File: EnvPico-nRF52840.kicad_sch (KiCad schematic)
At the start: 48 parts, among them J3 2.54mm header 01x20, J4 2.54mm header 01x20, J5 Conn_01x03_Male, U1 LM3671MF 3.3, U2 BQ24072RGT, U3 nRF52840, Y1 32MHz 12pF

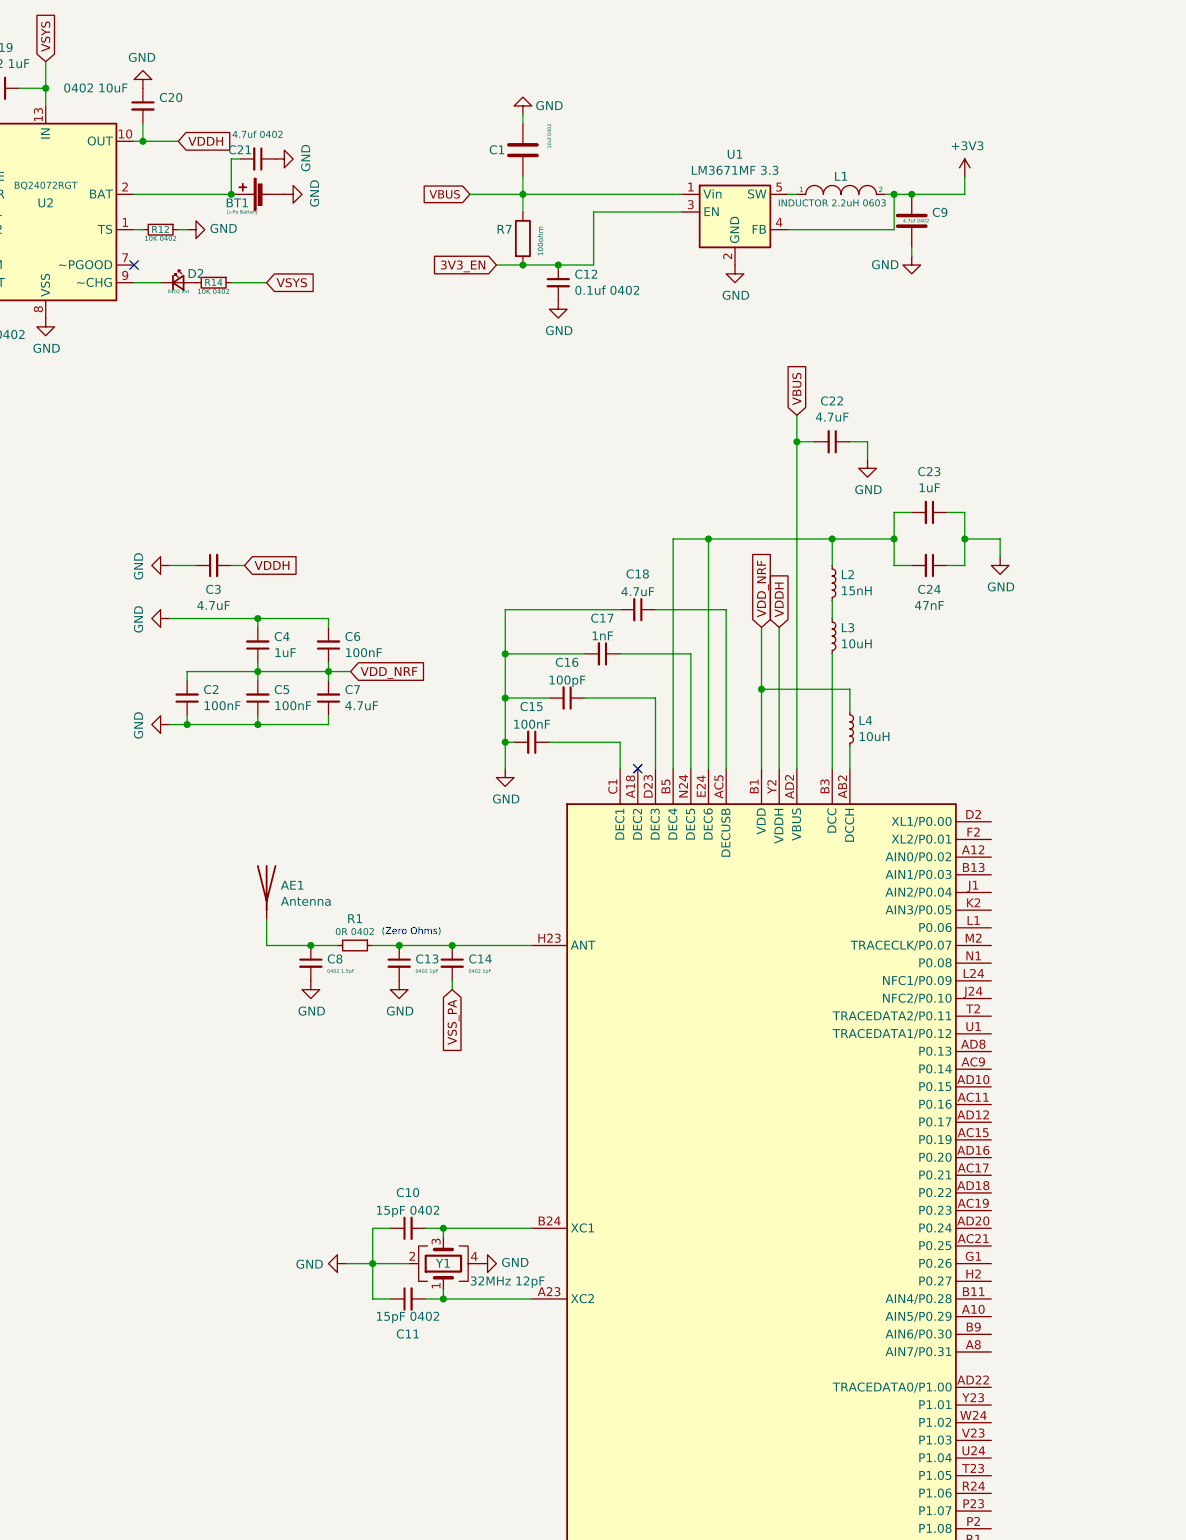
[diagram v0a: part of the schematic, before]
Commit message: started adding some pins for GPIO
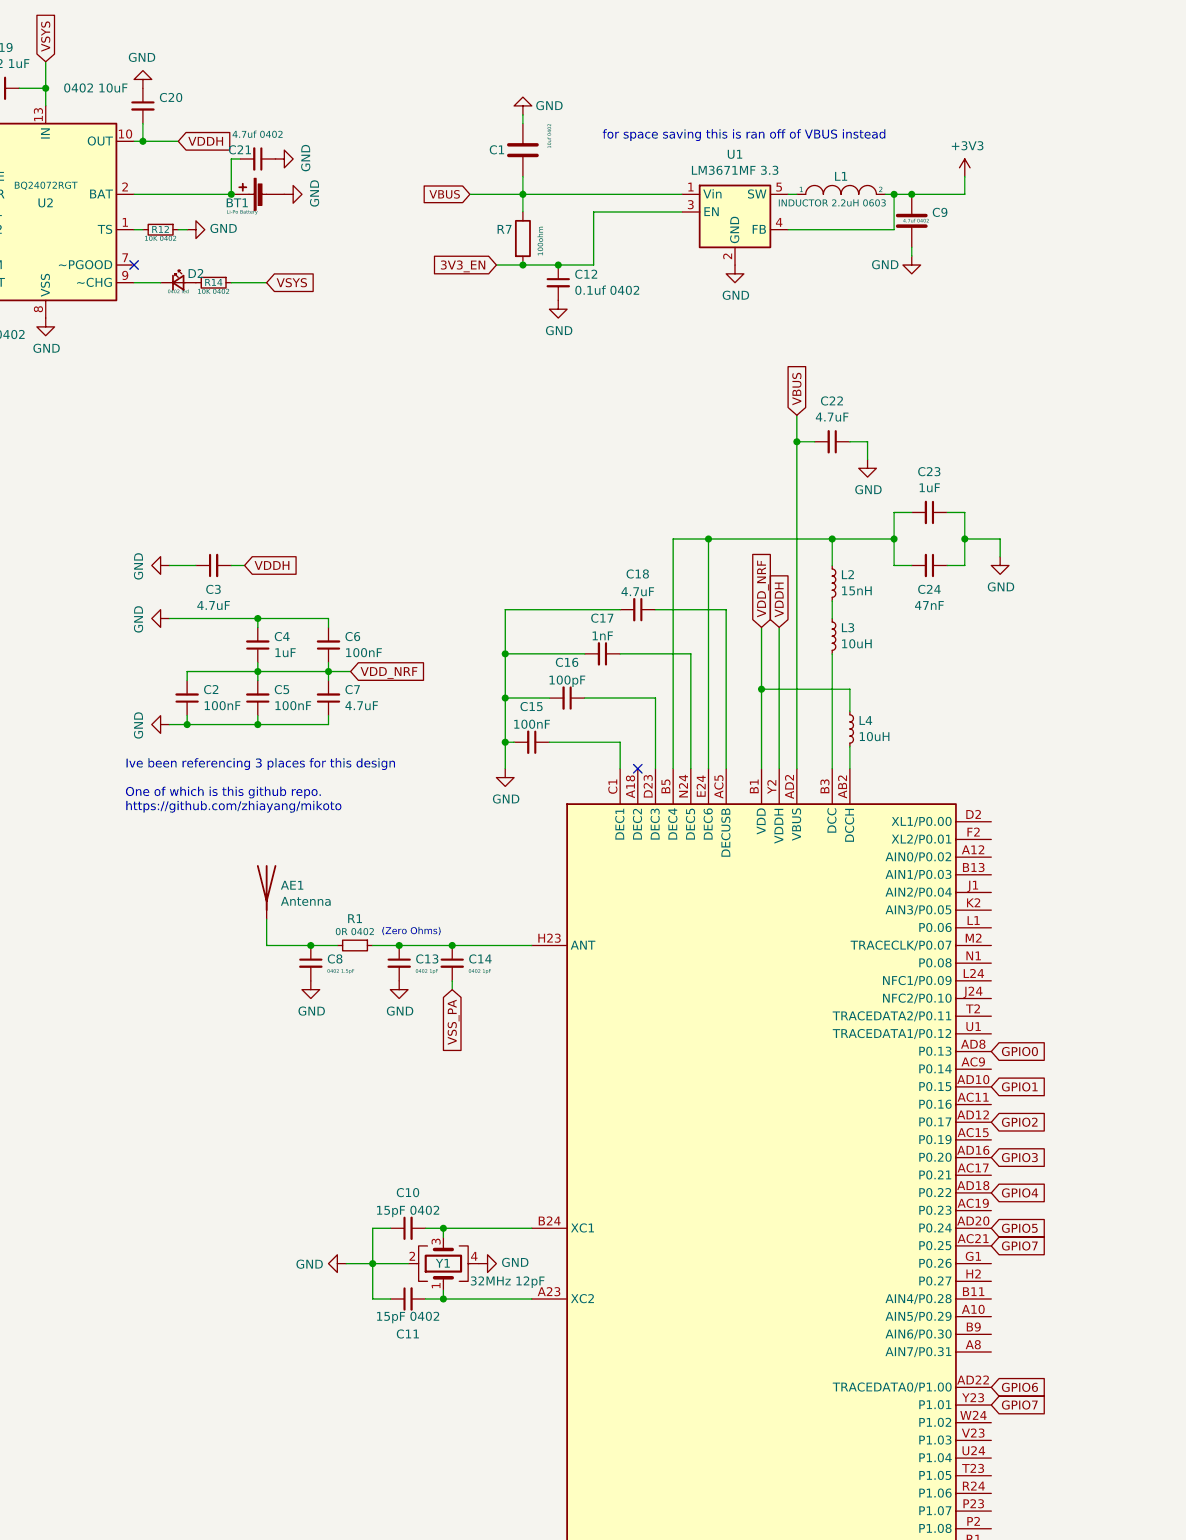
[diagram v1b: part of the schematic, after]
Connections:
- net GPIO7: now reaches U3.AC21 (P0.25)
- net GPIO7: now also U3.Y23 (P1.01)
- net GPIO1: now reaches U3.AD10 (P0.15)
- net GPIO2: now reaches U3.AD12 (P0.17)
- net GPIO3: now reaches U3.AD16 (P0.20)
- net GPIO4: now reaches U3.AD18 (P0.22)
- net GPIO5: now reaches U3.AD20 (P0.24)
- net GPIO6: now reaches U3.AD22 (TRACEDATA0/P1.00)
- net GPIO0: now reaches U3.AD8 (P0.13)
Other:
- note added: "Ive been referencing 3 places for this design One of which is this github repo. https://github.com/zhiayang/mikoto"
- note added: "for space saving this is ran off of VBUS instead"
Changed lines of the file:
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@@
     (effects (font (size 0.508 0.508)) (justify left bottom))
+  )
+  (text "Ive been referencing 3 places for this design\n\nOne of which is this github repo.\nhttps://github.com/zhiayang/mikoto"
+    (at 114.3 135.89 0)
+    (effects (font (size 1.27 1.27)) (justify left bottom))
   )
   (text "(Zero Ohms)" (at 151.13 153.67 0)
     (effects (font (size 0.9906 0.9906)) (justify left bottom))
+  )
+  (text "for space saving this is ran off of VBUS instead" (at 182.88 39.37 0)
+    (effects (font (size 1.27 1.27)) (justify left bottom))
   )
   (text "GPIOs" (at 347.98 114.3 0)
@@
     )
   )
+  (global_label "GPIO0" (shape input) (at 238.76 170.18 0) (fields_autoplaced)
+    (effects (font (size 1.27 1.27)) (justify left))
+    (property "Intersheet References" "${INTERSHEET_REFS}" (id 0) (at 246.7182 170.1006 0)
+      (effects (font (size 1.27 1.27)) (justify left) hide)
+    )
+  )
+  (global_label "GPIO1" (shape input) (at 238.76 175.26 0) (fields_autoplaced)
+    (effects (font (size 1.27 1.27)) (justify left))
+    (property "Intersheet References" "${INTERSHEET_REFS}" (id 0) (at 246.7182 175.1806 0)
+      (effects (font (size 1.27 1.27)) (justify left) hide)
+    )
+  )
+  (global_label "GPIO2" (shape input) (at 238.76 180.34 0) (fields_autoplaced)
+    (effects (font (size 1.27 1.27)) (justify left))
+    (property "Intersheet References" "${INTERSHEET_REFS}" (id 0) (at 246.7182 180.2606 0)
+      (effects (font (size 1.27 1.27)) (justify left) hide)
+    )
+  )
+  (global_label "GPIO3" (shape input) (at 238.76 185.42 0) (fields_autoplaced)
+    (effects (font (size 1.27 1.27)) (justify left))
+    (property "Intersheet References" "${INTERSHEET_REFS}" (id 0) (at 246.7182 185.3406 0)
+      (effects (font (size 1.27 1.27)) (justify left) hide)
+    )
+  )
+  (global_label "GPIO4" (shape input) (at 238.76 190.5 0) (fields_autoplaced)
+    (effects (font (size 1.27 1.27)) (justify left))
+    (property "Intersheet References" "${INTERSHEET_REFS}" (id 0) (at 246.7182 190.4206 0)
+      (effects (font (size 1.27 1.27)) (justify left) hide)
+    )
+  )
+  (global_label "GPIO5" (shape input) (at 238.76 195.58 0) (fields_autoplaced)
+    (effects (font (size 1.27 1.27)) (justify left))
+    (property "Intersheet References" "${INTERSHEET_REFS}" (id 0) (at 246.7182 195.5006 0)
+      (effects (font (size 1.27 1.27)) (justify left) hide)
+    )
+  )
+  (global_label "GPIO7" (shape input) (at 238.76 198.12 0) (fields_autoplaced)
+    (effects (font (size 1.27 1.27)) (justify left))
+    (property "Intersheet References" "${INTERSHEET_REFS}" (id 0) (at 246.7182 198.0406 0)
+      (effects (font (size 1.27 1.27)) (justify left) hide)
+    )
+  )
+  (global_label "GPIO6" (shape input) (at 238.76 218.44 0) (fields_autoplaced)
+    (effects (font (size 1.27 1.27)) (justify left))
+    (property "Intersheet References" "${INTERSHEET_REFS}" (id 0) (at 246.7182 218.3606 0)
+      (effects (font (size 1.27 1.27)) (justify left) hide)
+    )
+  )
+  (global_label "GPIO7" (shape input) (at 238.76 220.98 0) (fields_autoplaced)
+    (effects (font (size 1.27 1.27)) (justify left))
+    (property "Intersheet References" "${INTERSHEET_REFS}" (id 0) (at 246.7182 220.9006 0)
+      (effects (font (size 1.27 1.27)) (justify left) hide)
+    )
+  )

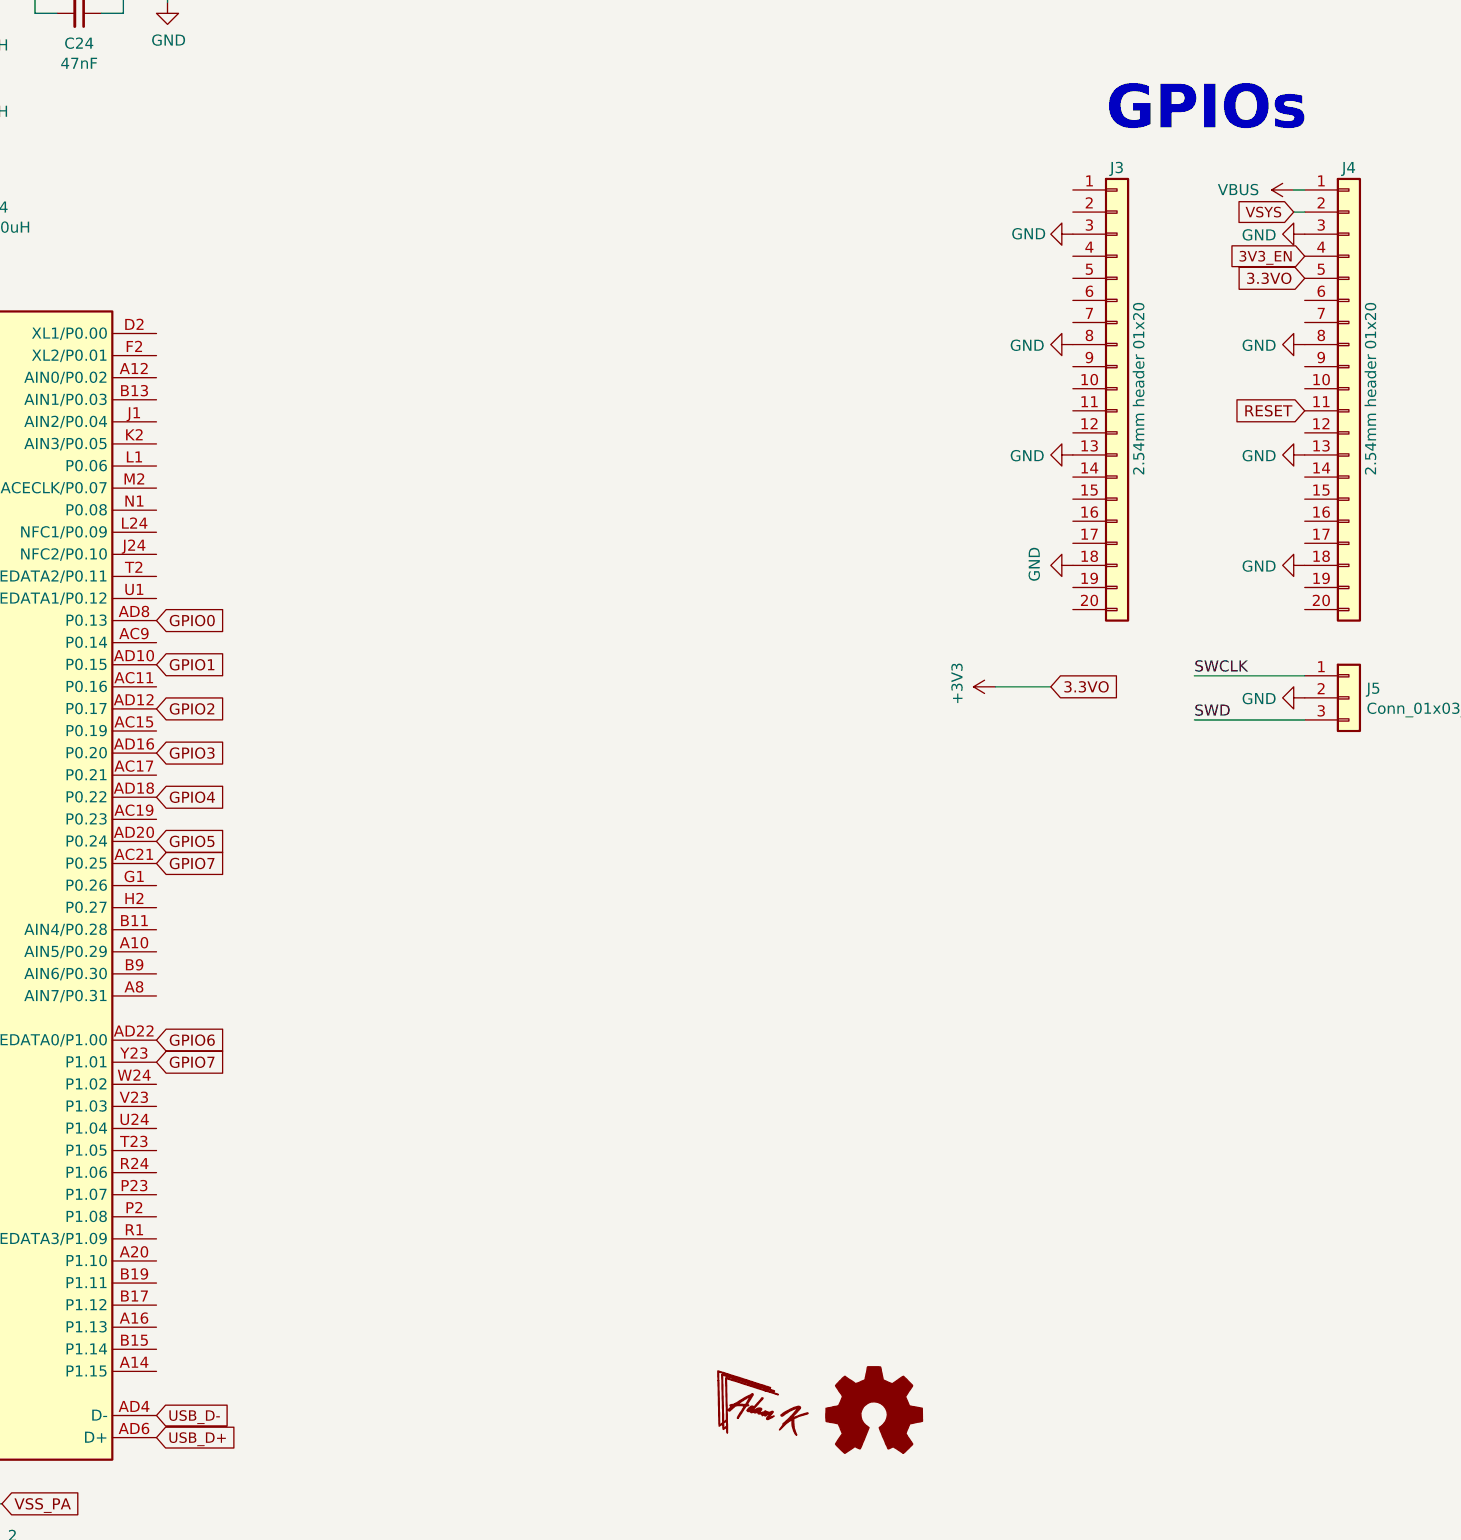
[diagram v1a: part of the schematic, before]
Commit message: connected all 26 GPIOs among other things.
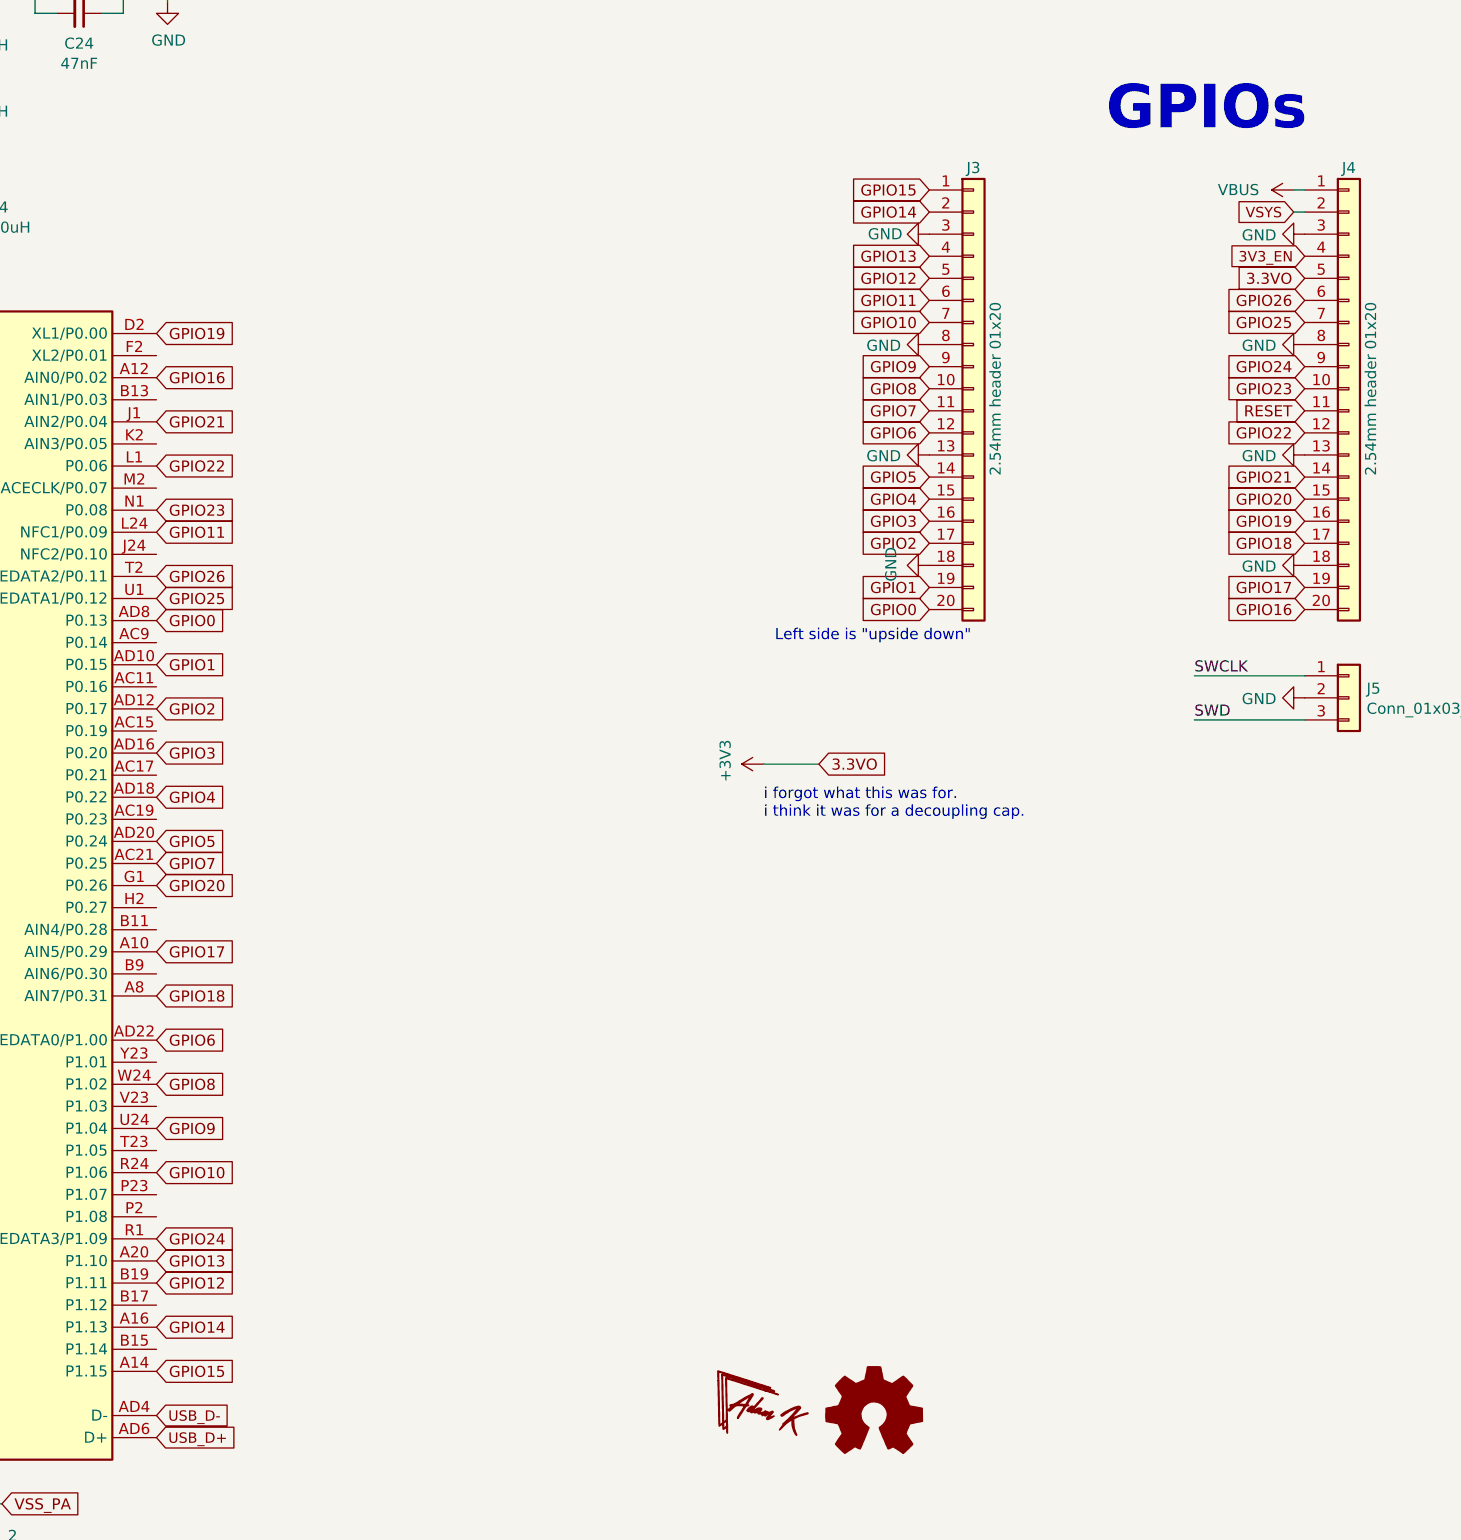
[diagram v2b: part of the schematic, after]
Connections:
- net GPIO0: now also J3.20 (Pin_20)
- net GPIO1: now also J3.19 (Pin_19)
- net GPIO2: now also J3.17 (Pin_17)
- net GPIO3: now also J3.16 (Pin_16)
- net GPIO4: now also J3.15 (Pin_15)
- net GPIO5: now also J3.14 (Pin_14)
- net GPIO6: now also J3.12 (Pin_12)
- net GPIO7: now also J3.11 (Pin_11); no longer U3.Y23 (P1.01)
- net GPIO23: now reaches J4.10 (Pin_10)
- net GPIO23: now also U3.N1 (P0.08)
- net GPIO22: now reaches J4.12 (Pin_12)
- net GPIO22: now also U3.L1 (P0.06)
- net GPIO21: now reaches J4.14 (Pin_14)
- net GPIO21: now also U3.J1 (AIN2/P0.04)
- net GPIO20: now reaches J4.15 (Pin_15)
- net GPIO20: now also U3.G1 (P0.26)
- net GPIO19: now reaches J4.16 (Pin_16)
- net GPIO19: now also U3.D2 (XL1/P0.00)
- net GPIO18: now reaches J4.17 (Pin_17)
- net GPIO18: now also U3.A8 (AIN7/P0.31)
- net GPIO17: now reaches J4.19 (Pin_19)
- net GPIO17: now also U3.A10 (AIN5/P0.29)
- net GPIO16: now reaches J4.20 (Pin_20)
- net GPIO16: now also U3.A12 (AIN0/P0.02)
- net GPIO26: now reaches J4.6 (Pin_6)
- net GPIO26: now also U3.T2 (TRACEDATA2/P0.11)
- net GPIO25: now reaches J4.7 (Pin_7)
- net GPIO25: now also U3.U1 (TRACEDATA1/P0.12)
- net GPIO24: now reaches J4.9 (Pin_9)
- net GPIO24: now also U3.R1 (TRACEDATA3/P1.09)
- net GPIO15: now reaches J3.1 (Pin_1)
- net GPIO15: now also U3.A14 (P1.15)
- net GPIO8: now reaches J3.10 (Pin_10)
- net GPIO8: now also U3.W24 (P1.02)
- net GPIO14: now reaches J3.2 (Pin_2)
- net GPIO14: now also U3.A16 (P1.13)
- net GPIO13: now reaches J3.4 (Pin_4)
- net GPIO13: now also U3.A20 (P1.10)
- net GPIO12: now reaches J3.5 (Pin_5)
- net GPIO12: now also U3.B19 (P1.11)
- net GPIO11: now reaches J3.6 (Pin_6)
- net GPIO11: now also U3.L24 (NFC1/P0.09)
- net GPIO10: now reaches J3.7 (Pin_7)
- net GPIO10: now also U3.R24 (P1.06)
- net GPIO9: now reaches J3.9 (Pin_9)
- net GPIO9: now also U3.U24 (P1.04)
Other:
- note added: "Left side is "upside down""
- note added: "i forgot what this was for. i think it was for a decoupling cap."
- moved on the sheet: J3
